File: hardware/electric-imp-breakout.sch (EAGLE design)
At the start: 22 parts, among them Q1 DMG2307L-7, U1 ELECTRIC_IMP, U2 TPS62172, U3 ATSHA204-TSU, X1 USBSMD

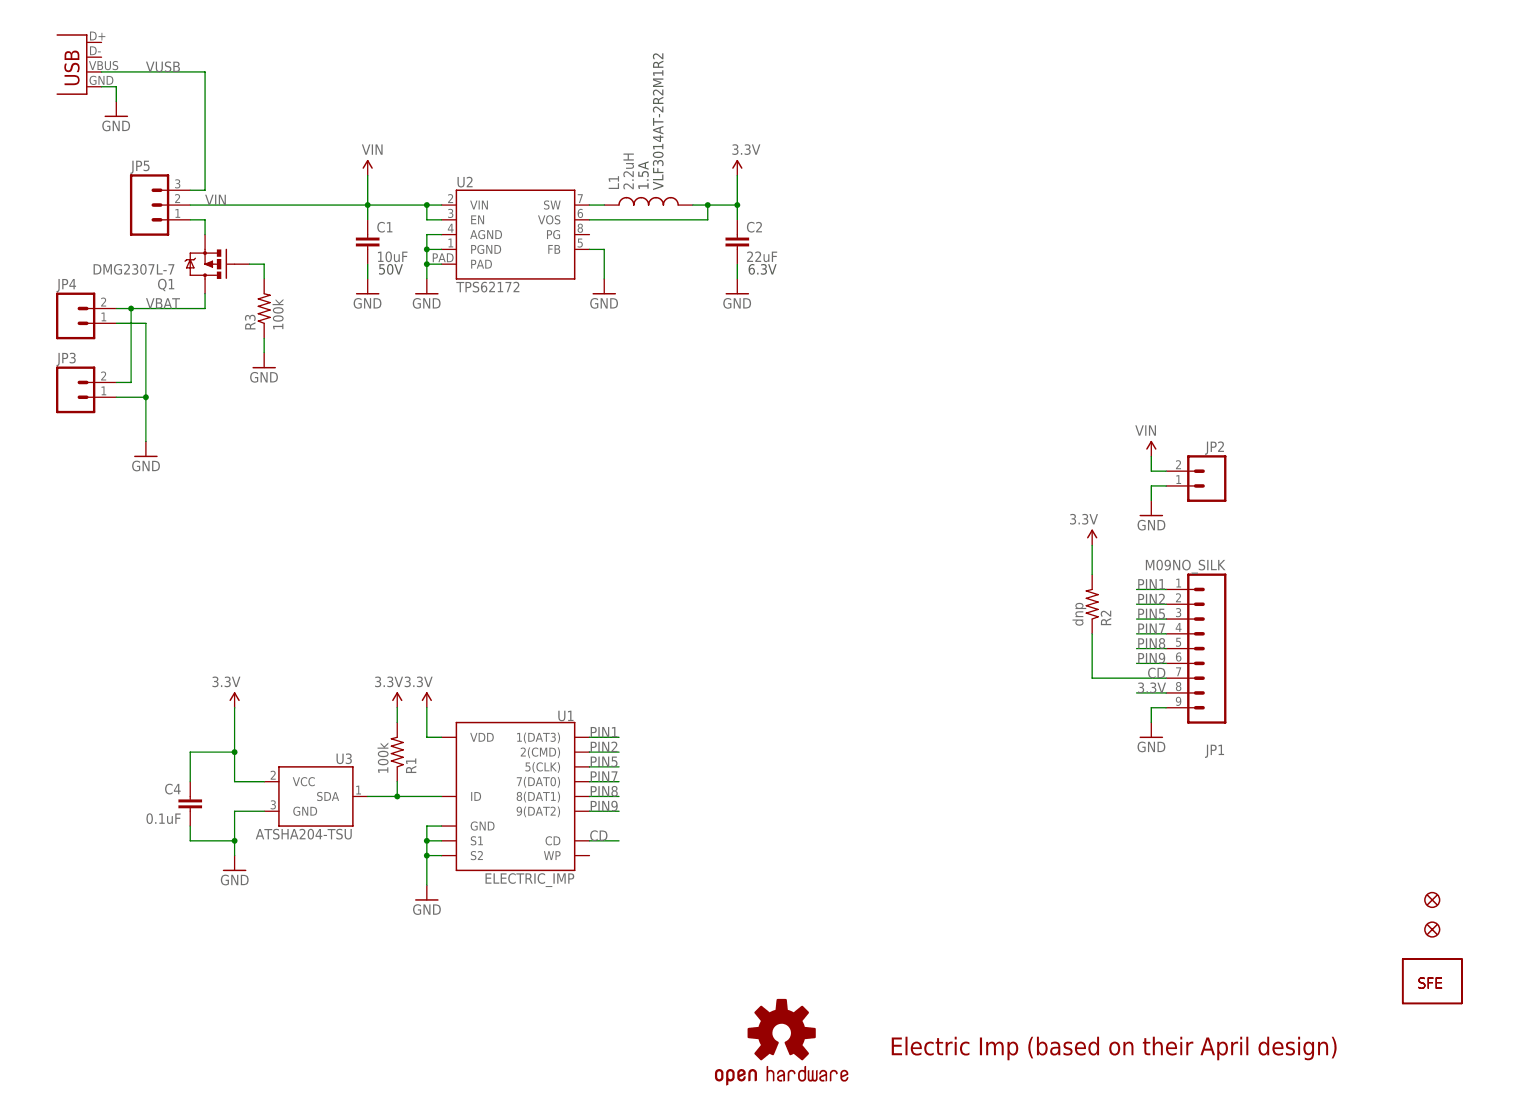
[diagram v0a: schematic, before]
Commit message: Changing to new socket FP, 0603 components, schematic updates
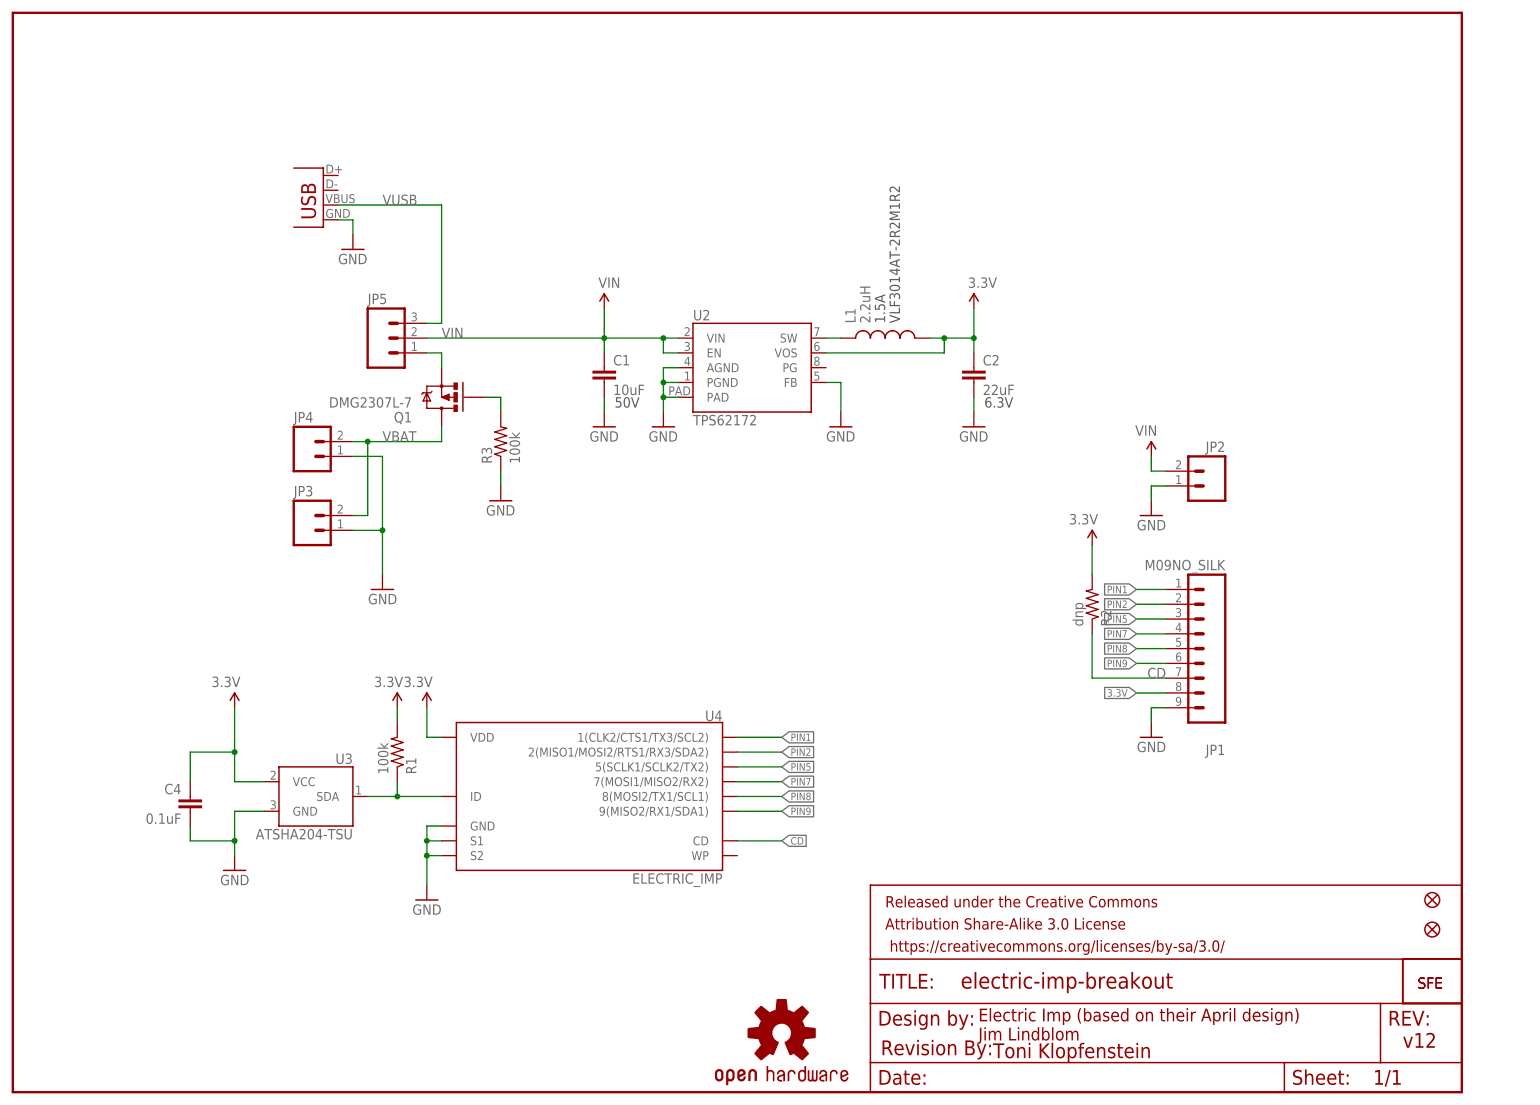
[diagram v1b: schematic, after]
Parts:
- removed U1: ELECTRIC_IMP, SparkFun-RF:ELECTRIC_IMP
- added FRAME1: FRAME-LETTER, SparkFun-Retired:FRAME-LETTER
- added U$3: REVISION, SparkFun-Aesthetics:REVISION
- added U4: ELECTRIC_IMP, SparkFun-RF:ELECTRIC_IMP
- C1: device SparkFun-Passives:CAP1210 -> SparkFun-Capacitors:10UF50V20%(1210)
- C2: device SparkFun-Passives:CAP0805 -> SparkFun-Capacitors:22UF-6.3V-20%(0805)
- C4: device SparkFun-Passives:CAP0402-CAP -> SparkFun-Capacitors:0.1UF-25V(+80/-20%)(0603)
- R1, R3: device SparkFun-Passives:RESISTOR0402-RES -> SparkFun-Resistors:100KOHM1/10W1%(0603)
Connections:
- net 3.3V: now also U4.VDD; no longer U1.VDD
- net CD: now also U4.CD; no longer U1.CD
- net GND: now also U4.GND, U4.S1, U4.S2; no longer U1.GND, U1.S1, U1.S2
- net ID: now also U4.ID; no longer U1.ID
- net PIN1: now also U4.1(CLK2/CTS1/TX3/SCL2); no longer U1.1(DAT3)
- net PIN2: now also U4.2(MISO1/MOSI2/RTS1/RX3/SDA2); no longer U1.2(CMD)
- net PIN5: now also U4.5(SCLK1/SCLK2/TX2); no longer U1.5(CLK)
- net PIN7: now also U4.7(MOSI1/MISO2/RX2); no longer U1.7(DAT0)
- net PIN8: now also U4.8(MOSI2/TX1/SCL1); no longer U1.8(DAT1)
- net PIN9: now also U4.9(MISO2/RX1/SDA1); no longer U1.9(DAT2)
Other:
- note added: "Electric Imp (based on their April design) Jim Lindblom"
- note added: "Toni Klopfenstein"
- note added: "v12"
- note removed: "Electric Imp (based on their April design)"
- moved on the sheet: C1, C2, JP3, JP4, JP5, L1, Q1, R3, U2

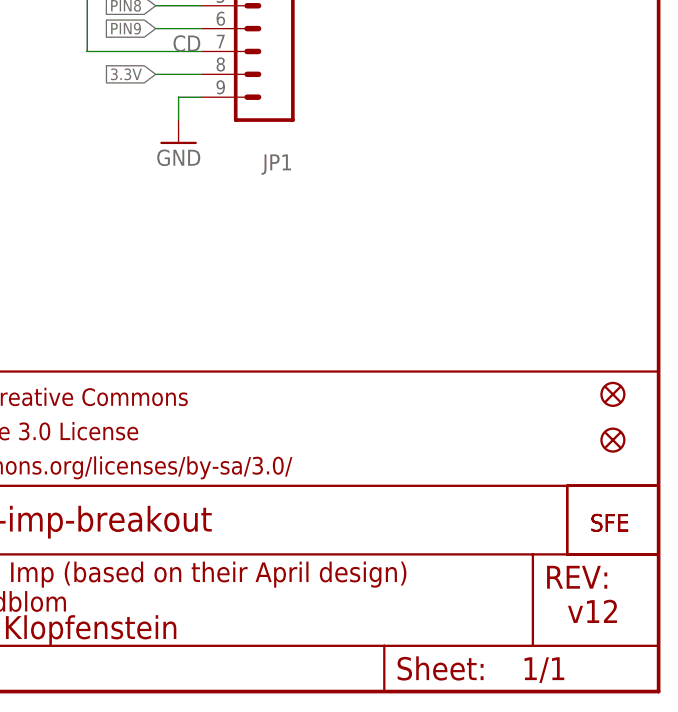
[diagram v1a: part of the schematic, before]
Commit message: Fixing DNP resistor to 0603, changing sparkfun logo
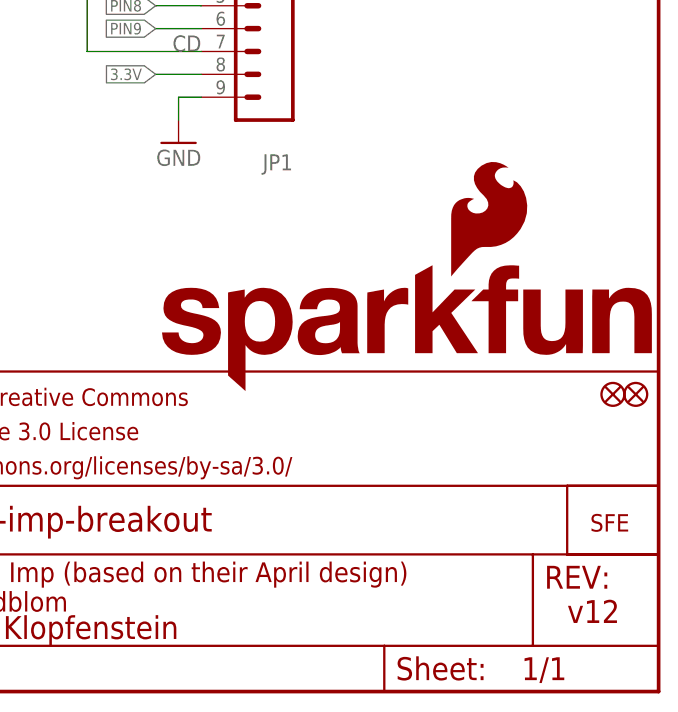
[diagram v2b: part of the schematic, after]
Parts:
- JP7: value LOGO-SFENEW -> SFE_LOGO_NAME_FLAME.1_INCH; device SparkFun-Aesthetics:LOGO-SFENEW -> SparkFun-Aesthetics:SFE_LOGO_NAME_FLAME.1_INCH
- R2: device SparkFun-Passives:RESISTOR0402-RES -> SparkFun-Resistors:RESISTOR0603
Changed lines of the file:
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@@
 <part name="GND7" library="SparkFun-Aesthetics" deviceset="GND" device=""/>
 <part name="GND8" library="SparkFun-Aesthetics" deviceset="GND" device=""/>
-<part name="R2" library="SparkFun-Passives" deviceset="RESISTOR" device="0402-RES" value="dnp"/>
+<part name="R2" library="SparkFun-Resistors" deviceset="RESISTOR" device="0603" value="dnp"/>
 <part name="P+5" library="SparkFun-Aesthetics" deviceset="3.3V" device=""/>
 <part name="X1" library="SparkFun-Connectors" deviceset="USB" device="SMD"/>
@@
 <part name="JP3" library="SparkFun-Connectors" deviceset="M02" device="SMD"/>
 <part name="JP6" library="SparkFun-Aesthetics" deviceset="LOGO-SFE" device="SK"/>
-<part name="JP7" library="SparkFun-Aesthetics" deviceset="LOGO-SFE" device="NEW"/>
+<part name="JP7" library="SparkFun-Aesthetics" deviceset="SFE_LOGO_NAME_FLAME" device=".1_INCH" value="SFE_LOGO_NAME_FLAME.1_INCH"/>
 <part name="U$5" library="SparkFun-Aesthetics" deviceset="OSHW-LOGO" device="S"/>
 <part name="JP8" library="SparkFun" deviceset="FIDUCIAL" device="UFIDUCIAL"/>
@@
 <instance part="JP3" gate="G$1" x="50.8" y="96.52"/>
 <instance part="JP6" gate="G$1" x="241.3" y="17.78"/>
-<instance part="JP7" gate="G$1" x="241.3" y="17.78"/>
+<instance part="JP7" gate="G$1" x="193.04" y="33.02"/>
 <instance part="U$5" gate="G$1" x="132.08" y="10.16"/>
 <instance part="JP8" gate="G$1" x="243.84" y="33.02"/>
-<instance part="JP9" gate="G$1" x="243.84" y="27.94"/>
+<instance part="JP9" gate="G$1" x="246.38" y="33.02"/>
 <instance part="U$3" gate="G$1" x="149.098" y="6.35"/>
 <instance part="U4" gate="G$1" x="99.06" y="50.8" rot="MR0"/>

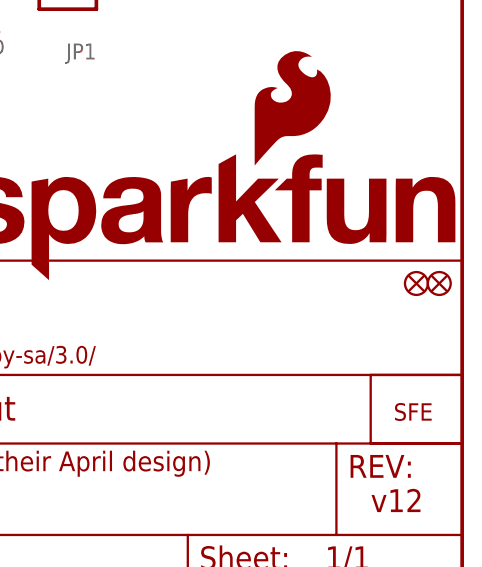
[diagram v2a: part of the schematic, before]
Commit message: removed micro fids, added regular
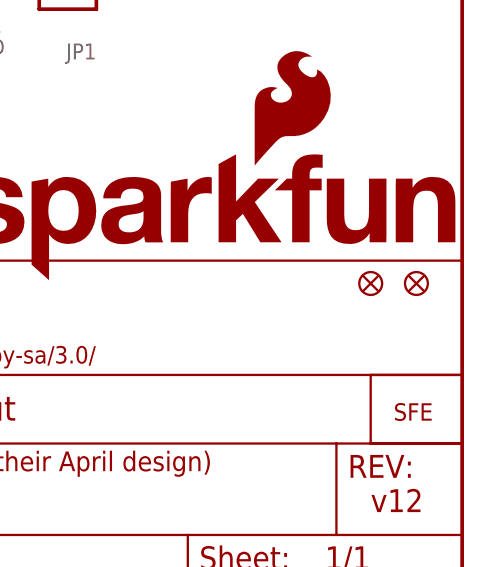
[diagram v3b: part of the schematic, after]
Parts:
- removed JP8, JP9: FIDUCIALUFIDUCIAL, SparkFun:FIDUCIALUFIDUCIAL
- added FID1, FID2: FIDUCIAL1X2, SparkFun-Aesthetics:FIDUCIAL1X2
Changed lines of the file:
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@@
 <?xml version="1.0" encoding="utf-8"?>
 <!DOCTYPE eagle SYSTEM "eagle.dtd">
-<eagle version="6.5.0">
+<eagle version="6.6.0">
 <drawing>
 <settings>
@@
 <part name="JP7" library="SparkFun-Aesthetics" deviceset="SFE_LOGO_NAME_FLAME" device=".1_INCH" value="SFE_LOGO_NAME_FLAME.1_INCH"/>
 <part name="U$5" library="SparkFun-Aesthetics" deviceset="OSHW-LOGO" device="S"/>
-<part name="JP8" library="SparkFun" deviceset="FIDUCIAL" device="UFIDUCIAL"/>
-<part name="JP9" library="SparkFun" deviceset="FIDUCIAL" device="UFIDUCIAL"/>
 <part name="U$3" library="SparkFun-Aesthetics" deviceset="REVISION" device=""/>
 <part name="U4" library="SparkFun-RF" deviceset="ELECTRIC_IMP" device=""/>
+<part name="FID1" library="SparkFun-Aesthetics" deviceset="FIDUCIAL" device="1X2"/>
+<part name="FID2" library="SparkFun-Aesthetics" deviceset="FIDUCIAL" device="1X2"/>
 </parts>
 <sheets>
@@
 <instance part="JP7" gate="G$1" x="193.04" y="33.02"/>
 <instance part="U$5" gate="G$1" x="132.08" y="10.16"/>
-<instance part="JP8" gate="G$1" x="243.84" y="33.02"/>
-<instance part="JP9" gate="G$1" x="246.38" y="33.02"/>
 <instance part="U$3" gate="G$1" x="149.098" y="6.35"/>
 <instance part="U4" gate="G$1" x="99.06" y="50.8" rot="MR0"/>
+<instance part="FID1" gate="G$1" x="243.84" y="33.02"/>
+<instance part="FID2" gate="G$1" x="238.76" y="33.02"/>
 </instances>
 <busses>
